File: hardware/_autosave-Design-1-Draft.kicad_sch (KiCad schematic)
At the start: 37 parts, among them J1 Barrel_Jack_Switch, M1 WATERPUMP-1, M2 WATERPUMP-2, Q1 IRLZ44N, Q2 IRLZ44N, Q3 PN2222A, SW1 Button, U3 ADS1115, U5 Tang_Nano_9K, U7 BOB-12009

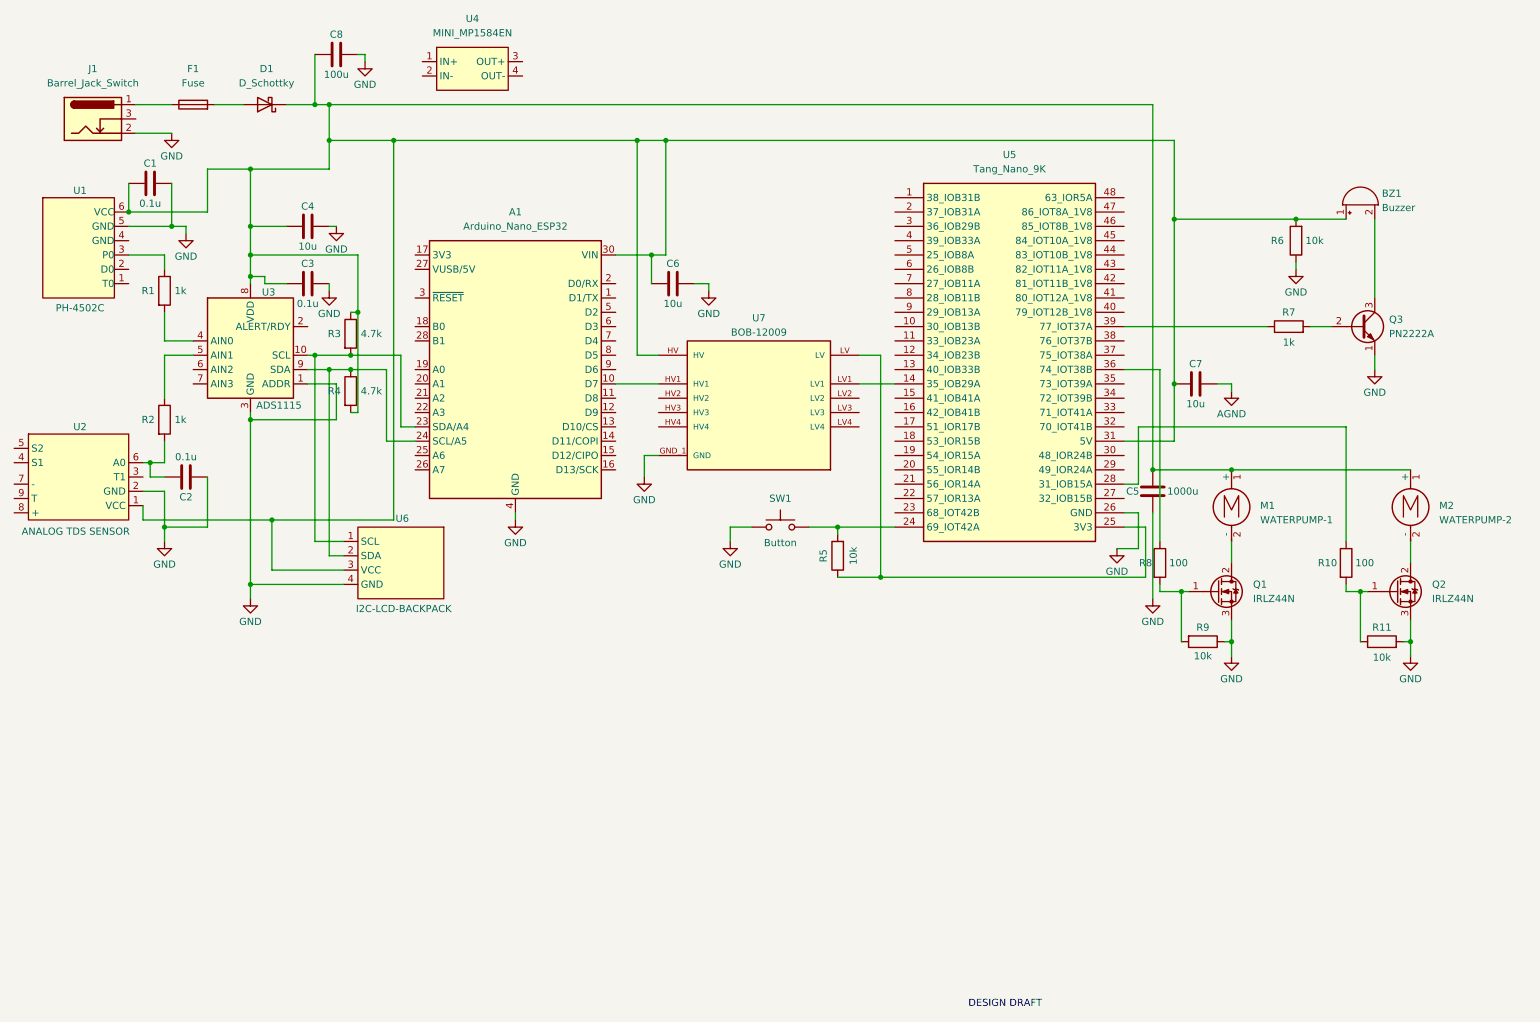
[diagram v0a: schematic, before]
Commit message: schem: buck converter added > one ground plane pcb: NEW component placement, need traces and ground fills
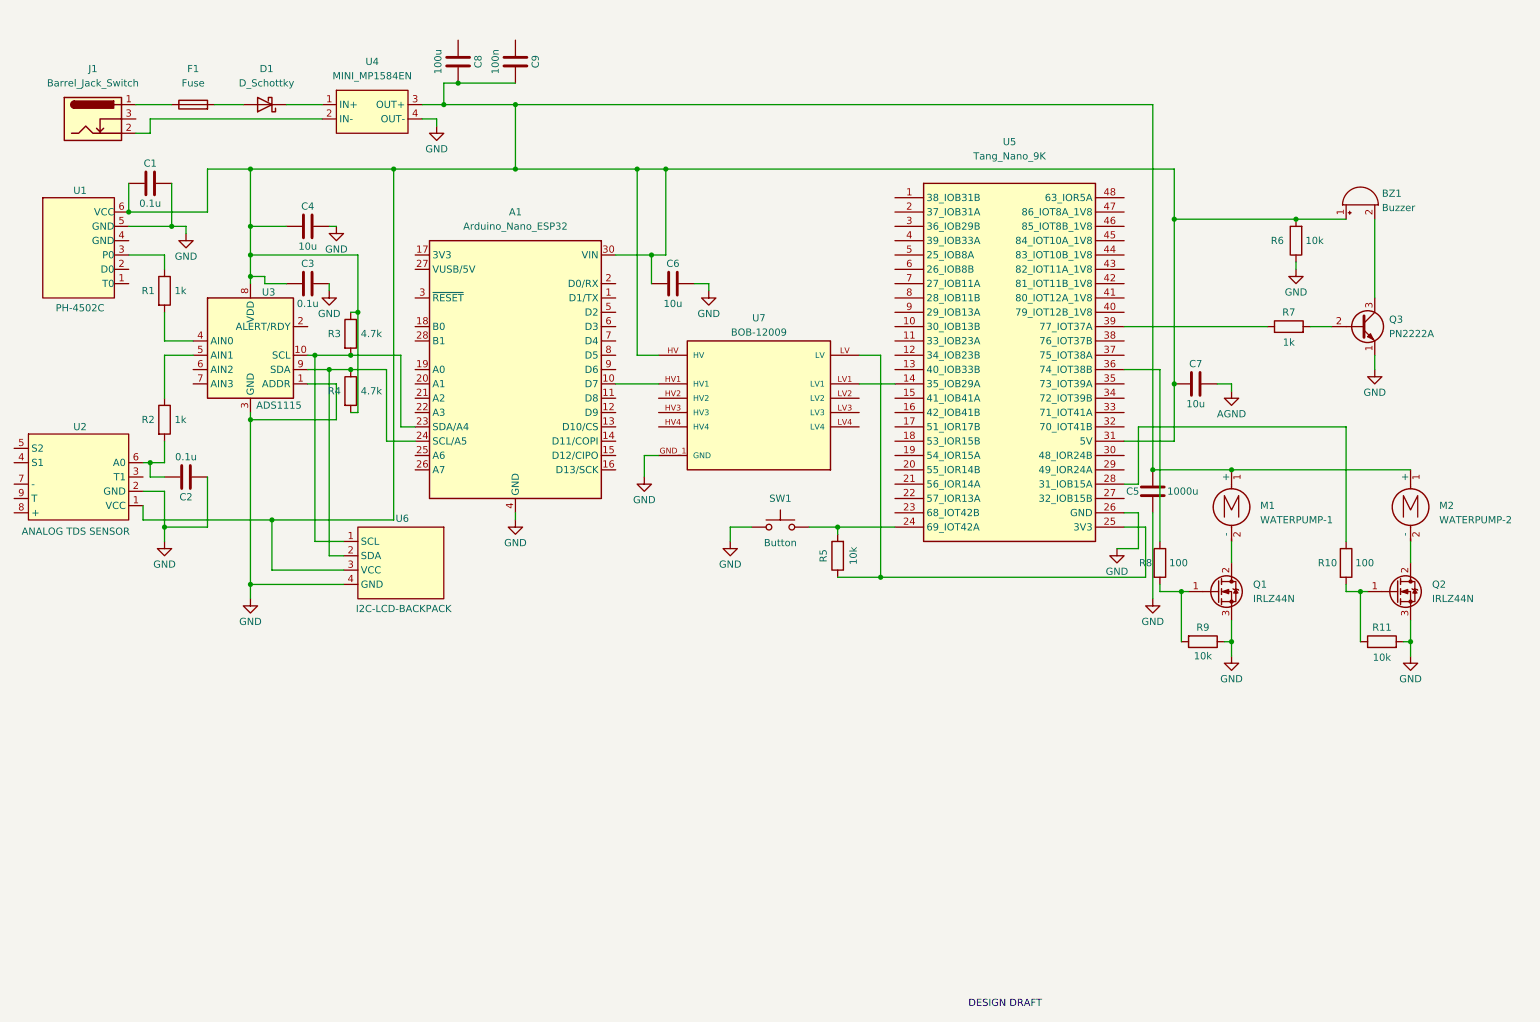
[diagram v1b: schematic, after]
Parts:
- added C9: 100n, Capacitor_THT:C_Radial_D6.3mm_H5.0mm_P2.50mm, symbol Device:C
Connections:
- net GND: now also U4.4 (OUT-); no longer C8.2, J1.2
- net at A1.30 (VIN), BZ1.1 (+), C1.1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: now also C8.2, U4.3 (OUT+), C9.2; no longer C8.1, D1.1 (K)
- net at U4.1 (IN+): now also D1.1 (K)
- net at U4.2 (IN-): now also J1.2
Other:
- moved on the sheet: C8, U4
